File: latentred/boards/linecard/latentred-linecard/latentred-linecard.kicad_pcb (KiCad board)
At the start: 4 copper layers, 220 x 92 mm, 453 parts, among them J1 CONN_LATENTRED_LINECARD_DEVICE, J2 STEWART_SS_74500_024, Q1 SSM6N58NU, Q2 SSM6N58NU, Q3 SSM6N58NU, Q4 SSM6N58NU, Q5 SSM6N58NU, Q6 SSM6N58NU, Q7 SSM6N58NU, Q8 SSM6N58NU, U1 MCP1703T-3302E, U10 DP83867, U11 DP83867, U12 DP83867, U13 DP83867, U14 DP83867, U15 DP83867, U16 DSC6101CI2A-025.0000, U17 5PB1108CMG, U2 LTC3374-QFN, U3 SI7050, U4 LTC2451, U5 INA226, U6 INA226, U7 INA226, U8 DP83867, U9 DP83867

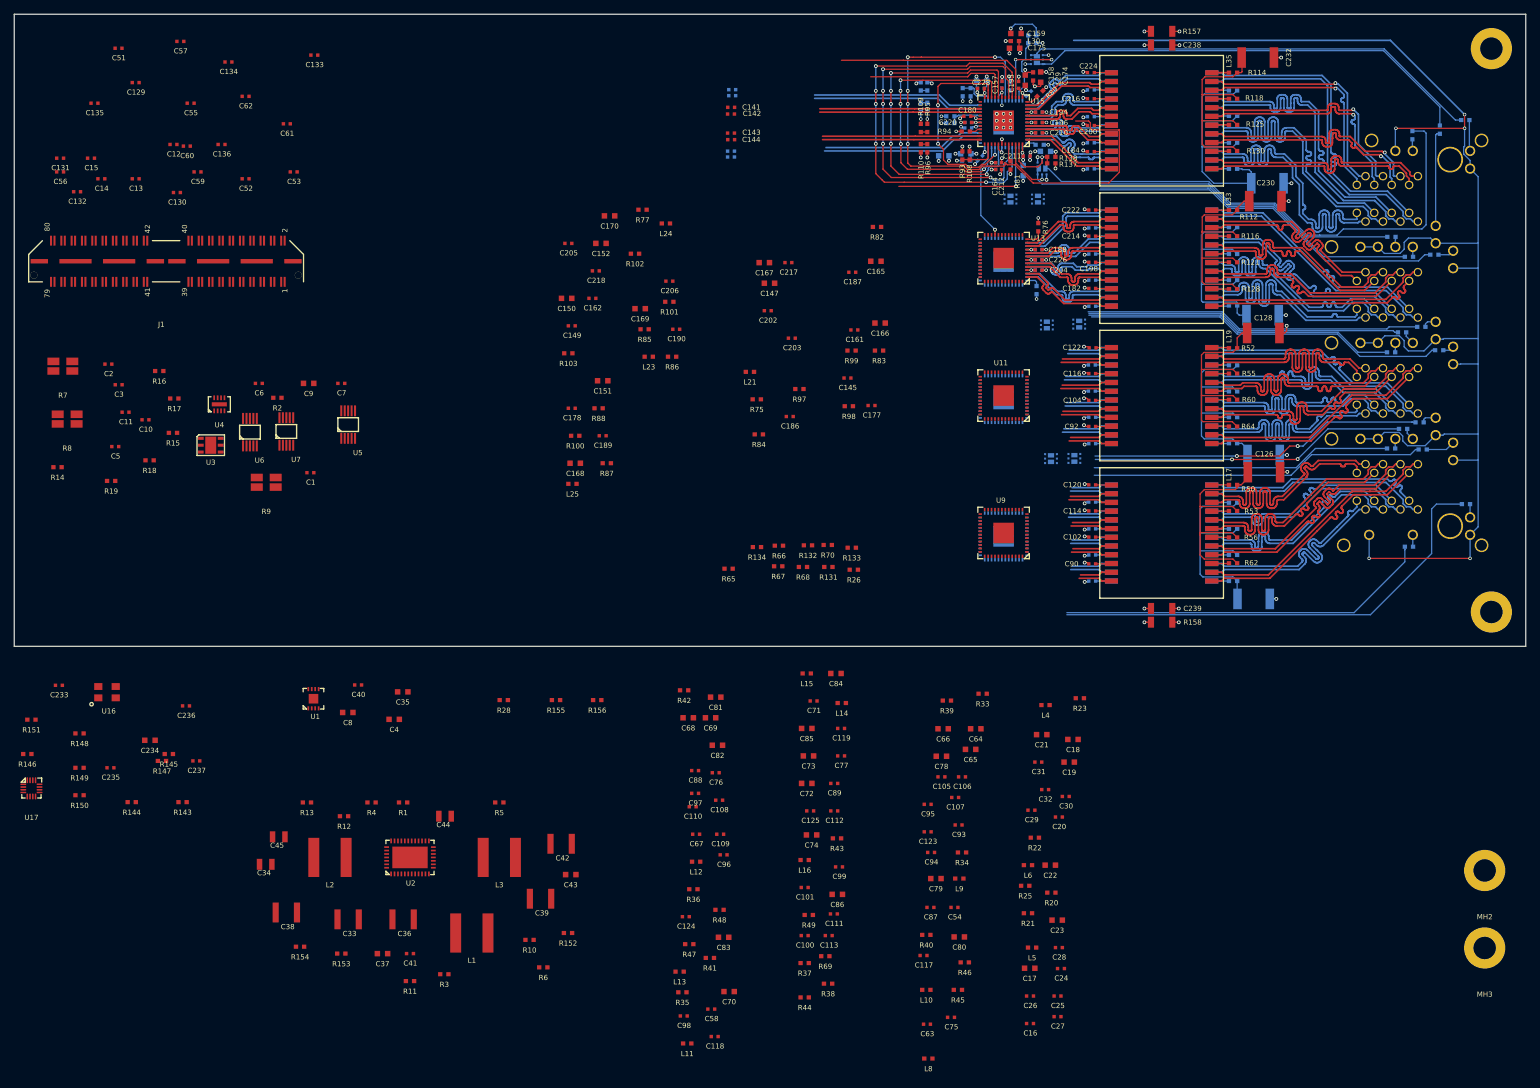
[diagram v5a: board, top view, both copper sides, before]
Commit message: Laid out second pair of PHYs
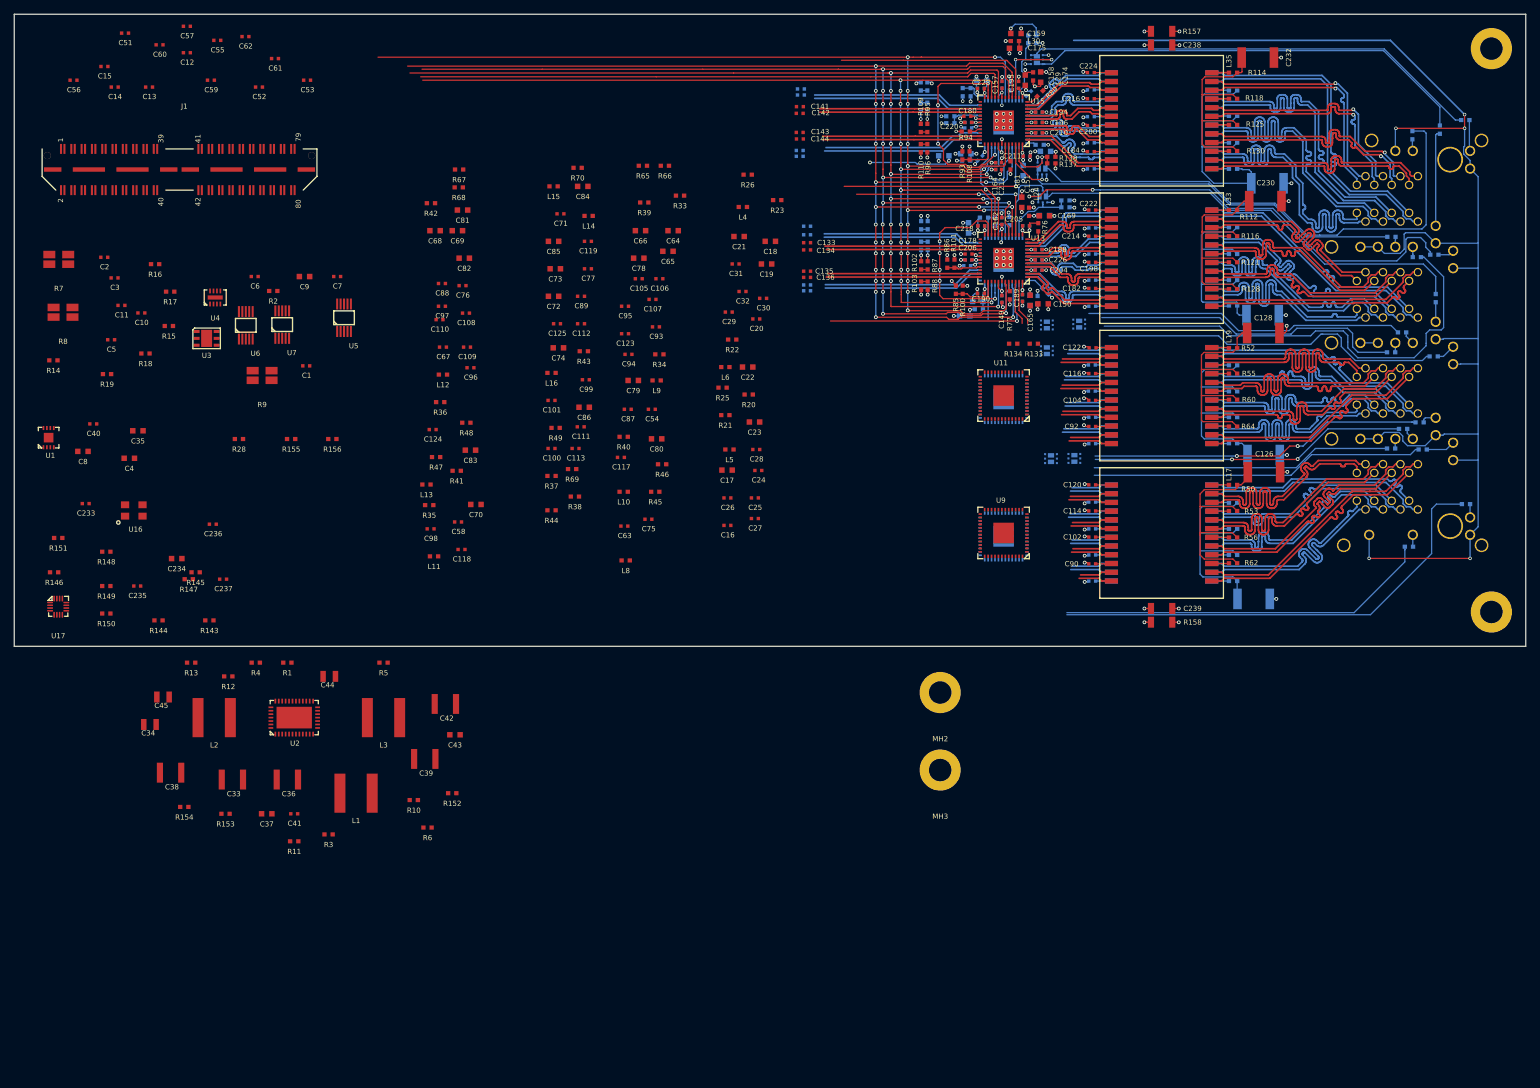
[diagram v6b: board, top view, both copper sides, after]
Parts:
- removed C147: 4.7 uF, azonenberg_pcb:EIA_0603_CAP_NOSILK
- removed L21: 600R, azonenberg_pcb:EIA_0402_RES_NOSILK
- C129, C130, C131, C132, C145, C152, C161, C166, C167, C168, C170, C177, C186, C187, C202, C203, C217, L23, L25, R131, R132, R75, R82, R83, R84, R97, R98, R99: moved to B.Cu
- moved C131 109.3 mm to (172.4, 45.6), turned to 180 degrees
- moved C135 106.6 mm to (172.4, 50.9), turned to 180 degrees
- moved C132 106.4 mm to (172.4, 44.4), turned to 180 degrees
- moved C129 102.1 mm to (172.4, 52.9), turned to 180 degrees
- moved C130 92.8 mm to (172.4, 53.8), turned to 180 degrees
- moved C134 88.6 mm to (172.4, 47.8), turned to 180 degrees
- moved C136 87.4 mm to (172.4, 51.8), turned to 180 degrees
- moved C79 84.8 mm to (147.1, 66.8)
- moved C80 84.8 mm to (150.5, 75.3)
- moved L9 84.8 mm to (150.5, 66.8)
- moved C105 84.8 mm to (147.9, 52.0)
- moved C106 84.8 mm to (150.9, 52.0)
- moved C107 84.8 mm to (149.9, 55.0)
- moved C117 84.8 mm to (145.3, 78.0)
- moved C123 84.8 mm to (145.9, 60.0)
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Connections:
- net /PHYs/RX_D2_4 renamed /PHYs/SGMII4_RX_C_P
- net /PHYs/RX_D2_5 renamed /PHYs/SGMII5_RX_C_P
- net /PHYs/RX_D3_4 renamed /PHYs/SGMII4_RX_C_N
- net /PHYs/RX_D3_5 renamed /PHYs/SGMII5_RX_C_N
- net Net-(C129-Pad1) renamed /PHYs/SGMII4_TX_C_P
- net Net-(C130-Pad1) renamed /PHYs/SGMII4_TX_C_N
- net Net-(C133-Pad1) renamed /PHYs/SGMII5_TX_C_P
- net Net-(C134-Pad1) renamed /PHYs/SGMII5_TX_C_N
- C166 pad 1: /PHYs/A1V8_4 -> /PHYs/A1V8_5
- C186 pad 1: /PHYs/A1V8_4 -> /PHYs/A1V8_5
- C202 pad 1: /PHYs/A1V8_4 -> /PHYs/A1V8_5
- U12 pad 13: /PHYs/A1V8_4 -> /PHYs/A1V8_5
- U12 pad 48: /PHYs/A1V8_4 -> /PHYs/A1V8_5
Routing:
- net /PHYs/1V8: track 105.8 -> 257.6 mm, vias 17 -> 31
- net /MGMT_MDC: track 64.6 -> 202.2 mm, vias 5 -> 17
- net /MGMT_MDIO: track 60.1 -> 193.8 mm, vias 5 -> 17
- net /JTAG_TCK: track 53.0 -> 182.6 mm, vias 5 -> 15
- net /JTAG_TMS: track 44.4 -> 168.9 mm, vias 5 -> 13
- net /GND: track 313.3 -> 435.5 mm, vias 86 -> 118
- net /PHY_RST_N: track 82.8 -> 188.8 mm, vias 5 -> 15
- net /PHYs/2V5: track 24.8 -> 112.7 mm, vias 1 -> 2
- net /PHYs/1V0: track 2.62 -> 84.0 mm, vias 2 -> 4
- net /JTAG_TDO: track 21.7 -> 87.2 mm
- net /PHYs/A1V0_5: track 2.40 -> 40.3 mm, vias 1 -> 7
- net /PHYs/CLK_25MHZ_4: track 0.00 -> 32.5 mm, vias 0 -> 1
- net /PHYs/CLK_25MHZ_5: track 0.00 -> 29.1 mm, vias 0 -> 2
- net /PHYs/JTAG_TDO_4: track 0.00 -> 28.9 mm, vias 0 -> 5
- net /PHYs/SGMII4_RX_C_P: track 0.00 -> 24.2 mm
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- added copper zone on In2.Cu, net /PHYs/1V8
- added copper zone on In2.Cu, net /PHYs/A1V0_7
- added copper zone on In2.Cu, net /PHYs/A1V8_7
- added copper zone on In2.Cu, net /PHYs/A2V5_7
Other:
- board text removed: "4"
- board text removed: "5"

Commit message: Initial layout on ports 2/3
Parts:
- removed C68, C69, C70: 4.7 uF, azonenberg_pcb:EIA_0603_CAP_NOSILK
- removed L11, L12, L13: 600R, azonenberg_pcb:EIA_0402_RES_NOSILK
- C108, C109, C110, C118, C124, C55, C56, C57, C58, C71, C76, C81, C82, C83, C88, C96, C97, C98, R35, R36, R41, R42, R47, R48, R67, R68, R69, R70: moved to B.Cu
- moved MH2 132.1 mm to (62.4, 85.2)
- moved MH3 132.1 mm to (62.4, 96.5)
- moved C56 118.9 mm to (173.8, 72.5), turned to 180 degrees
- moved C60 108.3 mm to (174.3, 67.7), turned to 180 degrees
- moved C57 105.1 mm to (174.0, 66.2), turned to 180 degrees
- moved C55 103.7 mm to (173.8, 73.4), turned to 180 degrees
- moved C59 98.9 mm to (174.3, 66.8), turned to 180 degrees
- moved C62 97.3 mm to (170.8, 72.0), turned to 180 degrees
- moved C61 91.2 mm to (170.8, 70.7), turned to 180 degrees
- moved C98 90.7 mm to (206.2, 69.2)
- moved R67 89.8 mm to (207.3, 63.5), turned to 180 degrees
- moved C81 89.8 mm to (206.5, 73.0)
- moved R68 88.9 mm to (207.3, 62.5)
- moved R35 87.9 mm to (204.8, 74.7), turned to 90 degrees
- moved C97 84.9 mm to (203.8, 63.9), turned to 90 degrees
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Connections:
- net Net-(C55-Pad1) renamed /PHYs/SGMII2_TX_C_P
- net Net-(C56-Pad1) renamed /PHYs/SGMII2_TX_C_N
- net Net-(C57-Pad1) renamed /PHYs/SGMII2_RX_C_P
- net Net-(C58-Pad1) renamed /PHYs/SGMII2_RX_C_N
- net Net-(C59-Pad1) renamed /PHYs/SGMII3_TX_C_P
- net Net-(C60-Pad1) renamed /PHYs/SGMII3_TX_C_N
- net Net-(C61-Pad1) renamed /PHYs/SGMII3_RX_C_P
- net Net-(C62-Pad1) renamed /PHYs/SGMII3_RX_C_N
- C108 pad 1: /PHYs/A2V5_2 -> /PHYs/A2V5_3
- C109 pad 1: /PHYs/A1V8_2 -> /PHYs/A1V8_3
- C110 pad 1: /PHYs/A1V0_2 -> /PHYs/A1V0_3
- C118 pad 1: /PHYs/A1V0_2 -> /PHYs/A1V0_3
- C124 pad 1: /PHYs/A1V0_2 -> /PHYs/A1V0_3
- C81 pad 1: /PHYs/A2V5_2 -> /PHYs/A2V5_3
- C82 pad 1: /PHYs/A1V8_2 -> /PHYs/A1V8_3
- C83 pad 1: /PHYs/A1V0_2 -> /PHYs/A1V0_3
- C96 pad 1: /PHYs/A2V5_2 -> /PHYs/A2V5_3
- C97 pad 1: /PHYs/A1V8_2 -> /PHYs/A1V8_3
- C98 pad 1: /PHYs/A1V0_2 -> /PHYs/A1V0_3
- L18 pad 11: /PHYs/ETH2_A_P -> /PHYs/ETH2_A_N
- L18 pad 12: /PHYs/ETH2_A_N -> /PHYs/ETH2_A_P
- L18 pad 2: /PHYs/ETH2_D_P -> /PHYs/ETH2_D_N
- L18 pad 3: /PHYs/ETH2_D_N -> /PHYs/ETH2_D_P
- L18 pad 5: /PHYs/ETH2_C_P -> /PHYs/ETH2_C_N
- L18 pad 6: /PHYs/ETH2_C_N -> /PHYs/ETH2_C_P
- L18 pad 8: /PHYs/ETH2_B_P -> /PHYs/ETH2_B_N
- L18 pad 9: /PHYs/ETH2_B_N -> /PHYs/ETH2_B_P
- L19 pad 11: /PHYs/ETH3_A_P -> /PHYs/ETH3_A_N
- L19 pad 12: /PHYs/ETH3_A_N -> /PHYs/ETH3_A_P
- L19 pad 2: /PHYs/ETH3_D_P -> /PHYs/ETH3_D_N
- L19 pad 3: /PHYs/ETH3_D_N -> /PHYs/ETH3_D_P
- L19 pad 5: /PHYs/ETH3_C_P -> /PHYs/ETH3_C_N
- L19 pad 6: /PHYs/ETH3_C_N -> /PHYs/ETH3_C_P
- L19 pad 8: /PHYs/ETH3_B_P -> /PHYs/ETH3_B_N
- L19 pad 9: /PHYs/ETH3_B_N -> /PHYs/ETH3_B_P
- U10 pad 13: /PHYs/A1V8_2 -> /PHYs/A1V8_3
- U10 pad 24: /PHYs/A1V0_2 -> /PHYs/A1V0_3
- U10 pad 3: /PHYs/A2V5_2 -> /PHYs/A2V5_3
- U10 pad 31: /PHYs/A1V0_2 -> /PHYs/A1V0_3
- U10 pad 42: /PHYs/A1V0_2 -> /PHYs/A1V0_3
- U10 pad 48: /PHYs/A1V8_2 -> /PHYs/A1V8_3
- U10 pad 6: /PHYs/A1V0_2 -> /PHYs/A1V0_3
- U10 pad 9: /PHYs/A2V5_2 -> /PHYs/A2V5_3
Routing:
- net /PHYs/1V8: track 257.6 -> 400.5 mm, vias 31 -> 46
- net /GND: track 435.5 -> 569.1 mm, vias 118 -> 158
- net /PHY_RST_N: track 188.8 -> 248.4 mm, vias 15 -> 25
- net /JTAG_TMS: track 168.9 -> 221.8 mm, vias 13 -> 23
- net /JTAG_TCK: track 182.6 -> 233.3 mm, vias 15 -> 25
- net /MGMT_MDIO: track 193.8 -> 244.0 mm, vias 17 -> 26
- net /MGMT_MDC: track 202.2 -> 251.6 mm, vias 17 -> 24
- net /PHYs/A1V0_3: track 0.00 -> 41.9 mm, vias 0 -> 8
- net /PHYs/2V5: track 112.7 -> 147.6 mm, vias 2 -> 4
- net /PHYs/CLK_25MHZ_3: track 0.00 -> 33.7 mm
- net /PHYs/JTAG_TDO_2: track 0.00 -> 33.2 mm, vias 0 -> 5
- net /PHYs/SGMII3_RX_C_N: track 0.00 -> 25.5 mm
- net /PHYs/SGMII3_RX_C_P: track 0.00 -> 25.5 mm
- net /PHYs/SGMII2_TX_C_P: track 0.00 -> 23.3 mm
- net /PHYs/SGMII2_TX_C_N: track 0.00 -> 23.1 mm
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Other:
- board text removed: "2"
- board text removed: "3"

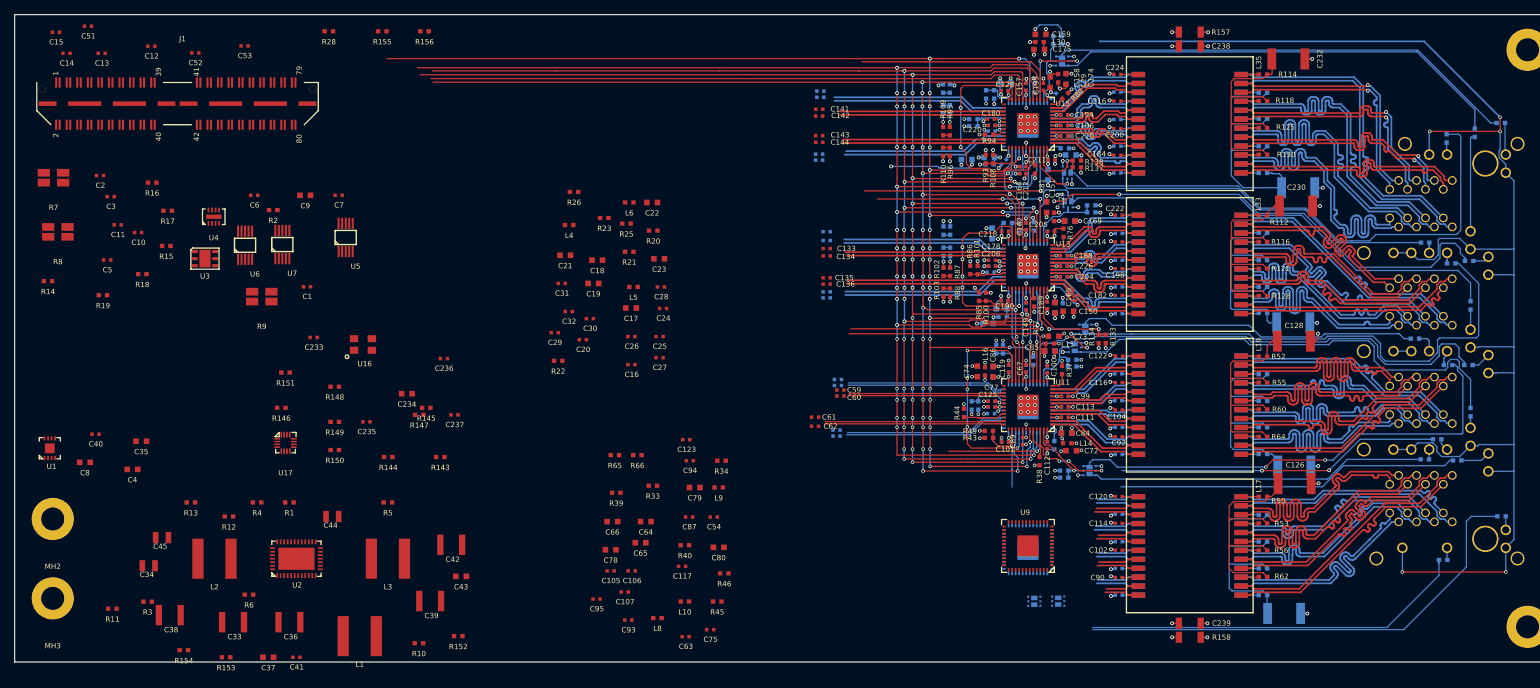
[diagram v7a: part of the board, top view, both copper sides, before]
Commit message: Continued PHY layout. Almost done with first pass but have a bunch of tweaking to do.
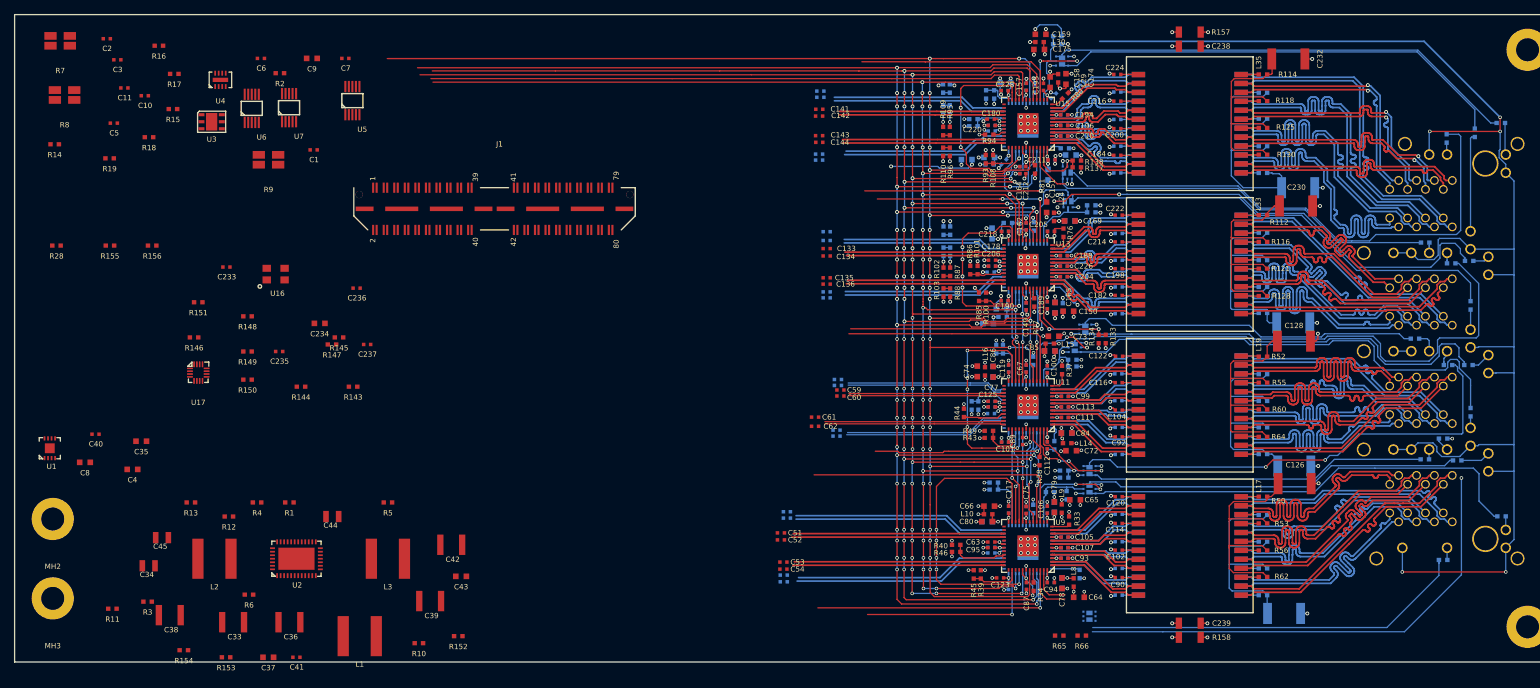
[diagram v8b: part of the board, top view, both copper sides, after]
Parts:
- removed C17, C18, C19: 4.7 uF, azonenberg_pcb:EIA_0603_CAP_NOSILK
- removed L4, L5, L6: 600R, azonenberg_pcb:EIA_0402_RES_NOSILK
- C12, C13, C14, C15, C16, C20, C21, C22, C23, C24, C25, C26, C27, C28, C29, C30, C31, C32, R20, R21, R22, R23, R25, R26: moved to B.Cu
- moved C15 124.2 mm to (166.8, 84.2), turned to 180 degrees
- moved C13 122.0 mm to (166.3, 93.2), turned to 180 degrees
- moved C51 122.0 mm to (165.9, 87.2), turned to 180 degrees
- moved C14 121.8 mm to (166.8, 85.0), turned to 180 degrees
- moved C12 117.8 mm to (166.3, 94.1), turned to 180 degrees
- moved C52 108.2 mm to (165.9, 88.2), turned to 180 degrees
- moved C53 106.0 mm to (166.2, 91.3), turned to 180 degrees
- moved C21 84.6 mm to (205.8, 94.3), turned to 270 degrees
- moved R26 80.0 mm to (204.2, 81.3)
- moved R20 77.8 mm to (208.3, 93.0), turned to 90 degrees
- moved C30 74.9 mm to (206.2, 89.2)
- moved C29 74.4 mm to (203.8, 83.8), turned to 90 degrees
- moved R25 73.5 mm to (206.5, 81.8), turned to 90 degrees
- moved C22 71.7 mm to (204.8, 83.5), turned to 90 degrees
- moved C31 71.6 mm to (195.8, 89.2), turned to 180 degrees
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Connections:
- net Net-(C12-Pad1) renamed /PHYs/SGMII0_TX_C_P
- net Net-(C13-Pad1) renamed /PHYs/SGMII0_TX_C_N
- net Net-(C14-Pad1) renamed /PHYs/SGMII0_RX_C_P
- net Net-(C15-Pad1) renamed /PHYs/SGMII0_RX_C_N
- net Net-(C51-Pad1) renamed /PHYs/SGMII1_TX_C_P
- net Net-(C52-Pad1) renamed /PHYs/SGMII1_TX_C_N
- net Net-(C53-Pad1) renamed /PHYs/SGMII1_RX_C_P
- net Net-(C54-Pad1) renamed /PHYs/SGMII1_RX_C_N
- C21 pad 1: /PHYs/A2V5_0 -> /PHYs/A2V5_1
- C22 pad 1: /PHYs/A1V8_0 -> /PHYs/A1V8_1
- C23 pad 1: /PHYs/A1V0_0 -> /PHYs/A1V0_1
- C25 pad 1: /PHYs/A2V5_0 -> /PHYs/A2V5_1
- C26 pad 1: /PHYs/A1V8_0 -> /PHYs/A1V8_1
- C27 pad 1: /PHYs/A1V0_0 -> /PHYs/A1V0_1
- C28 pad 1: /PHYs/A2V5_0 -> /PHYs/A2V5_1
- C29 pad 1: /PHYs/A1V8_0 -> /PHYs/A1V8_1
- C30 pad 1: /PHYs/A1V0_0 -> /PHYs/A1V0_1
- C31 pad 1: /PHYs/A1V0_0 -> /PHYs/A1V0_1
- C32 pad 1: /PHYs/A1V0_0 -> /PHYs/A1V0_1
- L17 pad 11: /PHYs/ETH1_A_P -> /PHYs/ETH1_A_N
- L17 pad 12: /PHYs/ETH1_A_N -> /PHYs/ETH1_A_P
- L17 pad 2: /PHYs/ETH1_D_P -> /PHYs/ETH1_D_N
- L17 pad 3: /PHYs/ETH1_D_N -> /PHYs/ETH1_D_P
- L17 pad 5: /PHYs/ETH1_C_P -> /PHYs/ETH1_C_N
- L17 pad 6: /PHYs/ETH1_C_N -> /PHYs/ETH1_C_P
- L17 pad 8: /PHYs/ETH1_B_P -> /PHYs/ETH1_B_N
- L17 pad 9: /PHYs/ETH1_B_N -> /PHYs/ETH1_B_P
- L7 pad 11: /PHYs/ETH0_A_P -> /PHYs/ETH0_A_N
- L7 pad 12: /PHYs/ETH0_A_N -> /PHYs/ETH0_A_P
- L7 pad 2: /PHYs/ETH0_D_P -> /PHYs/ETH0_D_N
- L7 pad 3: /PHYs/ETH0_D_N -> /PHYs/ETH0_D_P
- L7 pad 5: /PHYs/ETH0_C_P -> /PHYs/ETH0_C_N
- L7 pad 6: /PHYs/ETH0_C_N -> /PHYs/ETH0_C_P
- L7 pad 8: /PHYs/ETH0_B_P -> /PHYs/ETH0_B_N
- L7 pad 9: /PHYs/ETH0_B_N -> /PHYs/ETH0_B_P
- U8 pad 13: /PHYs/A1V8_0 -> /PHYs/A1V8_1
- U8 pad 24: /PHYs/A1V0_0 -> /PHYs/A1V0_1
- U8 pad 3: /PHYs/A2V5_0 -> /PHYs/A2V5_1
- U8 pad 31: /PHYs/A1V0_0 -> /PHYs/A1V0_1
- U8 pad 42: /PHYs/A1V0_0 -> /PHYs/A1V0_1
- U8 pad 48: /PHYs/A1V8_0 -> /PHYs/A1V8_1
- U8 pad 6: /PHYs/A1V0_0 -> /PHYs/A1V0_1
- U8 pad 9: /PHYs/A2V5_0 -> /PHYs/A2V5_1
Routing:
- net /GND: track 569.1 -> 694.9 mm, vias 158 -> 193
- net /MGMT_MDC: track 251.6 -> 306.7 mm, vias 24 -> 33
- net /MGMT_MDIO: track 244.0 -> 295.7 mm, vias 26 -> 33
- net /PHYs/1V8: track 400.5 -> 450.5 mm, vias 46 -> 57
- net /JTAG_TCK: track 233.3 -> 278.9 mm, vias 25 -> 34
- net /PHY_RST_N: track 248.4 -> 292.9 mm, vias 25 -> 30
- net /PHYs/JTAG_TDO_0: track 0.00 -> 43.8 mm, vias 0 -> 5
- net /PHYs/2V5: track 147.6 -> 189.6 mm, vias 4 -> 5
- net /JTAG_TMS: track 221.8 -> 261.4 mm, vias 23 -> 32
- net /PHYs/A1V0_1: track 0.00 -> 39.0 mm, vias 0 -> 7
- net /PHYs/CLK_25MHZ_1: track 0.00 -> 38.6 mm
- net /PHYs/CLK_25MHZ_0: track 0.00 -> 36.5 mm, vias 0 -> 1
- net /PHYs/SGMII0_TX_C_P: track 0.00 -> 30.5 mm
- net /PHYs/SGMII0_RX_C_P: track 0.00 -> 30.4 mm
- net /PHYs/SGMII0_RX_C_N: track 0.00 -> 30.4 mm
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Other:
- board text removed: "0"
- board text removed: "1"
